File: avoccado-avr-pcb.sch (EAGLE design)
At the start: 31 parts, among them IC1 MCP1703CB, Q1 #MHz, Q2 MOSFET-NCHANNEL2N7002PW, U1 ATMEGA168#, U2 MCP73831, X1 Micro USB

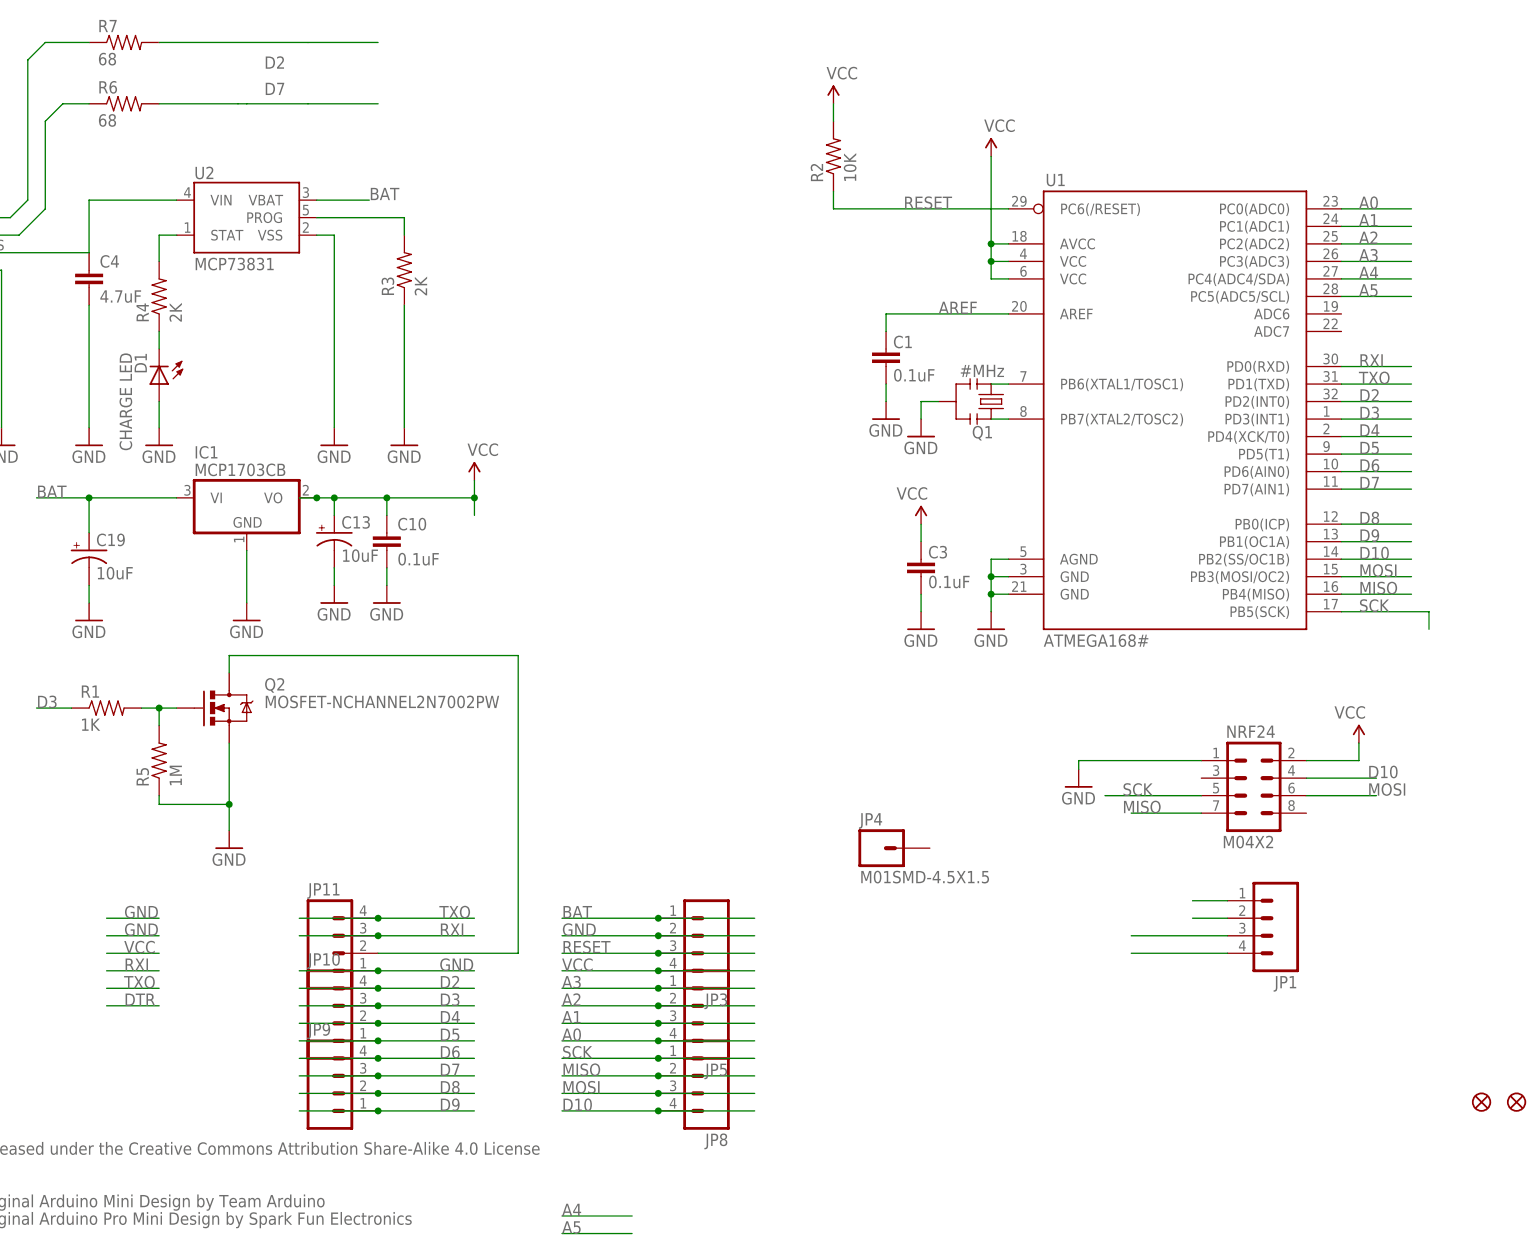
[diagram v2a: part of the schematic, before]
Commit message: white silkscreen fills at GND pads
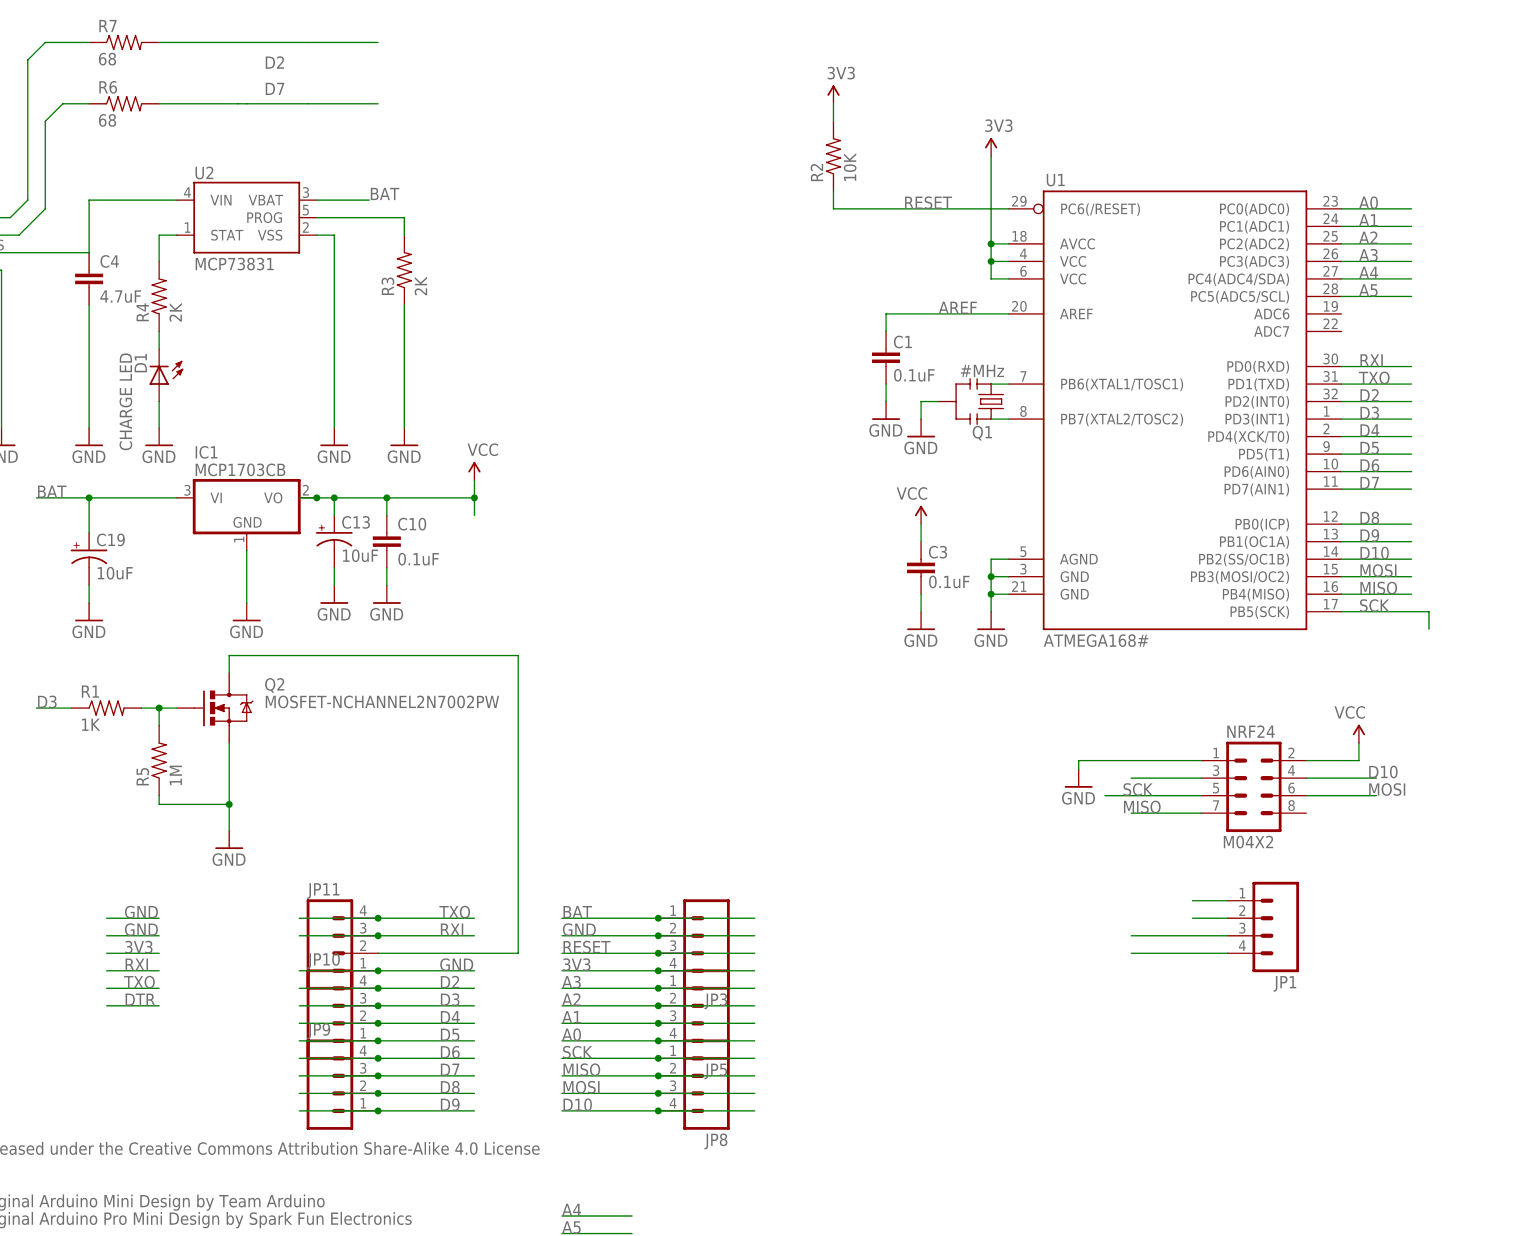
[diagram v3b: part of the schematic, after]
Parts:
- removed JP4: M01SMD-4.5X1.5, SparkFun-Connectors:M01SMD-4.5X1.5
- removed U$2, U$4: FIDUCIAL1X2, SparkFun:FIDUCIAL1X2
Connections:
- removed net 3.3V: NRF24.2
- removed net VCC: C10.1, C13.+, C3.2, IC1.VO, JP1.2, JP3.4, R2.2, U1.AVCC, U1.VCC@1, U1.VCC@2
- new net 3V3: C10.1, C13.+, C3.2, IC1.VO, JP1.2, JP3.4, NRF24.2, R2.2, U1.AVCC, U1.VCC@1, U1.VCC@2
- net D9: now also NRF24.3
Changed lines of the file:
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@@
 <part name="GND30" library="SparkFun" deviceset="GND" device=""/>
 <part name="GND32" library="SparkFun" deviceset="GND" device=""/>
-<part name="P+11" library="SparkFun" deviceset="3.3V" device="" value="VCC"/>
+<part name="P+11" library="SparkFun" deviceset="3.3V" device="" value="3V3"/>
 <part name="P+12" library="SparkFun" deviceset="3.3V" device="" value="VCC"/>
 <part name="P+15" library="SparkFun" deviceset="3.3V" device="" value="VCC"/>
-<part name="U$2" library="SparkFun" deviceset="FIDUCIAL" device="1X2"/>
-<part name="U$4" library="SparkFun" deviceset="FIDUCIAL" device="1X2"/>
 <part name="Q1" library="SparkFun" deviceset="RESONATOR" device="SMD" value="#MHz"/>
 <part name="GND4" library="SparkFun" deviceset="GND" device=""/>
 <part name="U1" library="SparkFun" deviceset="ATMEGA168" device="" value="ATMEGA168#"/>
-<part name="P+1" library="SparkFun" deviceset="3.3V" device="" value="VCC"/>
+<part name="P+1" library="SparkFun" deviceset="3.3V" device="" value="3V3"/>
 <part name="GND5" library="SparkFun" deviceset="GND" device=""/>
 <part name="Q2" library="SparkFun-DiscreteSemi" deviceset="MOSFET-NCHANNEL" device="2N7002PW"/>
@@
 <part name="GND9" library="SparkFun" deviceset="GND" device=""/>
 <part name="R5" library="SparkFun-Resistors" deviceset="RESISTOR" device="0603" value="1M"/>
-<part name="JP4" library="SparkFun-Connectors" deviceset="M01" device="SMD-4.5X1.5"/>
 <part name="JP3" library="smd-pads" deviceset="M04" device="SMD1X4"/>
 <part name="JP5" library="smd-pads" deviceset="M04" device="SMD1X4"/>
@@
 <attribute name="VALUE" x="151.384" y="112.776" size="1.778" layer="96"/>
 </instance>
-<instance part="U$2" gate="G$1" x="236.22" y="25.4"/>
-<instance part="U$4" gate="G$1" x="241.3" y="25.4"/>
 <instance part="Q1" gate="G$1" x="165.1" y="127" smashed="yes" rot="MR90">
 <attribute name="NAME" x="162.306" y="123.444" size="1.778" layer="95" rot="MR180"/>
@@
 <instance part="GND9" gate="1" x="54.61" y="62.23"/>
 <instance part="R5" gate="G$1" x="44.45" y="74.93" rot="R90"/>
-<instance part="JP4" gate="G$1" x="148.59" y="62.23"/>
 <instance part="JP3" gate="G$1" x="121.92" y="49.53" rot="R180"/>
 <instance part="JP5" gate="G$1" x="121.92" y="39.37" rot="R180"/>
@@
 </segment>
 </net>
-<net name="VCC" class="0">
+<net name="3V3" class="0">
 <segment>
 <wire x1="142.24" y1="170.18" x2="142.24" y2="167.64" width="0.1524" layer="91"/>
@@
 <pinref part="JP1" gate="G$1" pin="2"/>
 </segment>
+<segment>
+<pinref part="P+2" gate="G$1" pin="3.3V"/>
+<wire x1="218.44" y1="77.47" x2="218.44" y2="74.93" width="0.2032" layer="91"/>
+<pinref part="NRF24" gate="G$1" pin="2"/>
+<wire x1="218.44" y1="74.93" x2="210.82" y2="74.93" width="0.2032" layer="91"/>
+</segment>
 </net>
 <net name="D9" class="0">
@@
 <label x="218.44" y="106.68" size="1.778" layer="95"/>
 <pinref part="U1" gate="G$1" pin="PB1(OC1A)"/>
+</segment>
+<segment>
+<wire x1="185.42" y1="72.39" x2="195.58" y2="72.39" width="0.1524" layer="91"/>
+<pinref part="NRF24" gate="G$1" pin="3"/>
 </segment>
 </net>
@@
 </segment>
 </net>
-<net name="3.3V" class="0">
-<segment>
-<pinref part="P+2" gate="G$1" pin="3.3V"/>
-<wire x1="218.44" y1="77.47" x2="218.44" y2="74.93" width="0.2032" layer="91"/>
-<pinref part="NRF24" gate="G$1" pin="2"/>
-<wire x1="218.44" y1="74.93" x2="210.82" y2="74.93" width="0.2032" layer="91"/>
-</segment>
-</net>

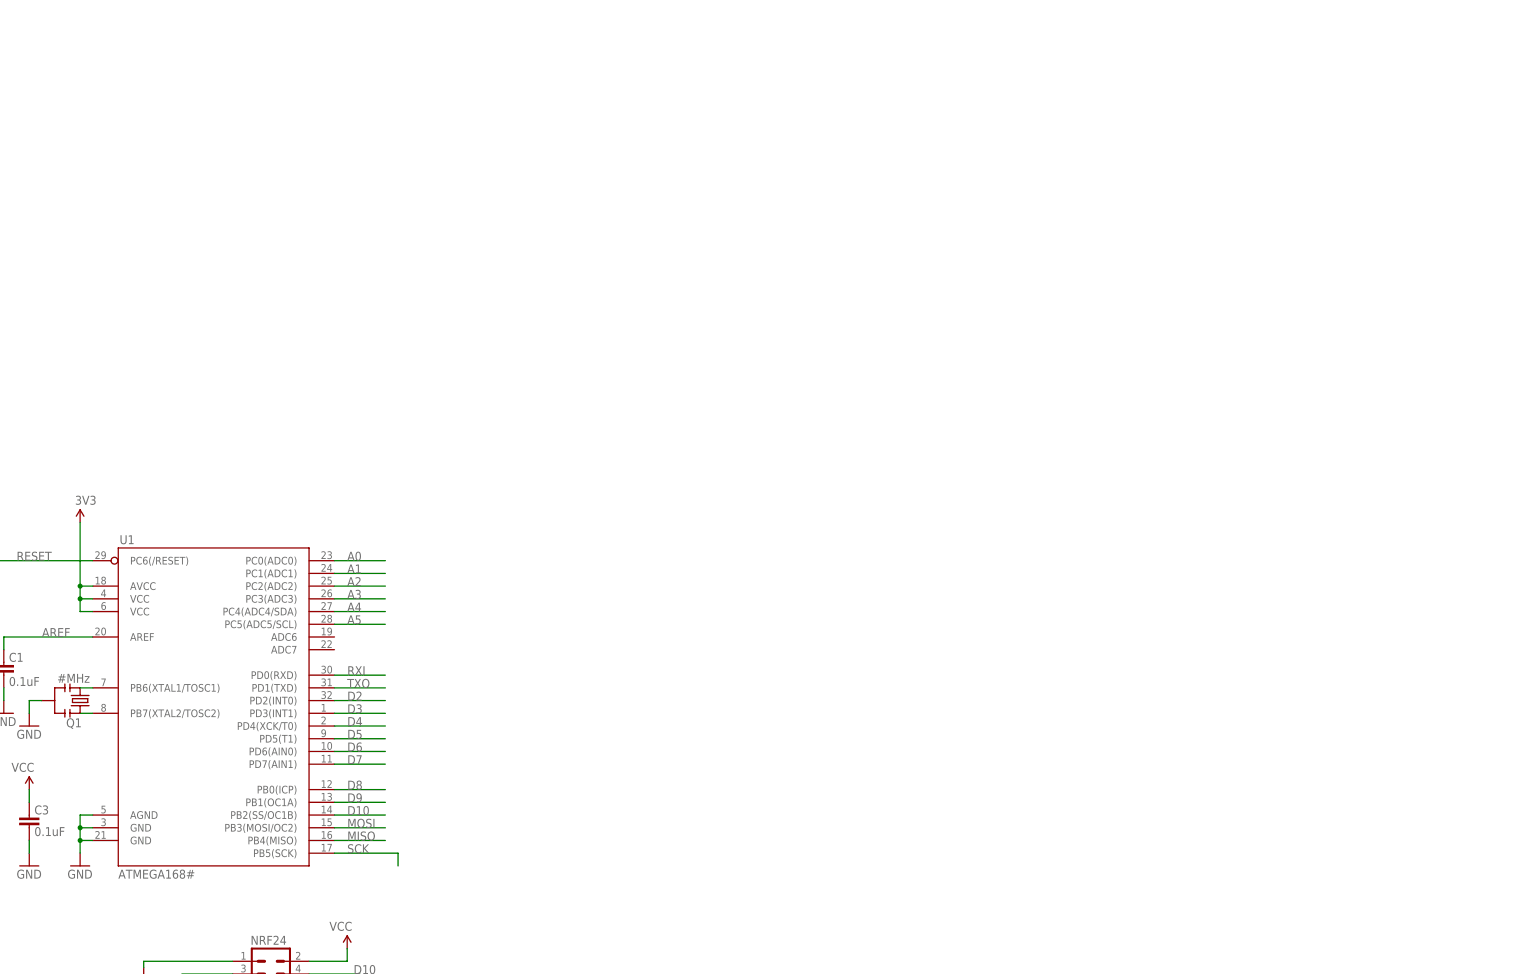
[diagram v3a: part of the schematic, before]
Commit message: add QFN package for MCU wip
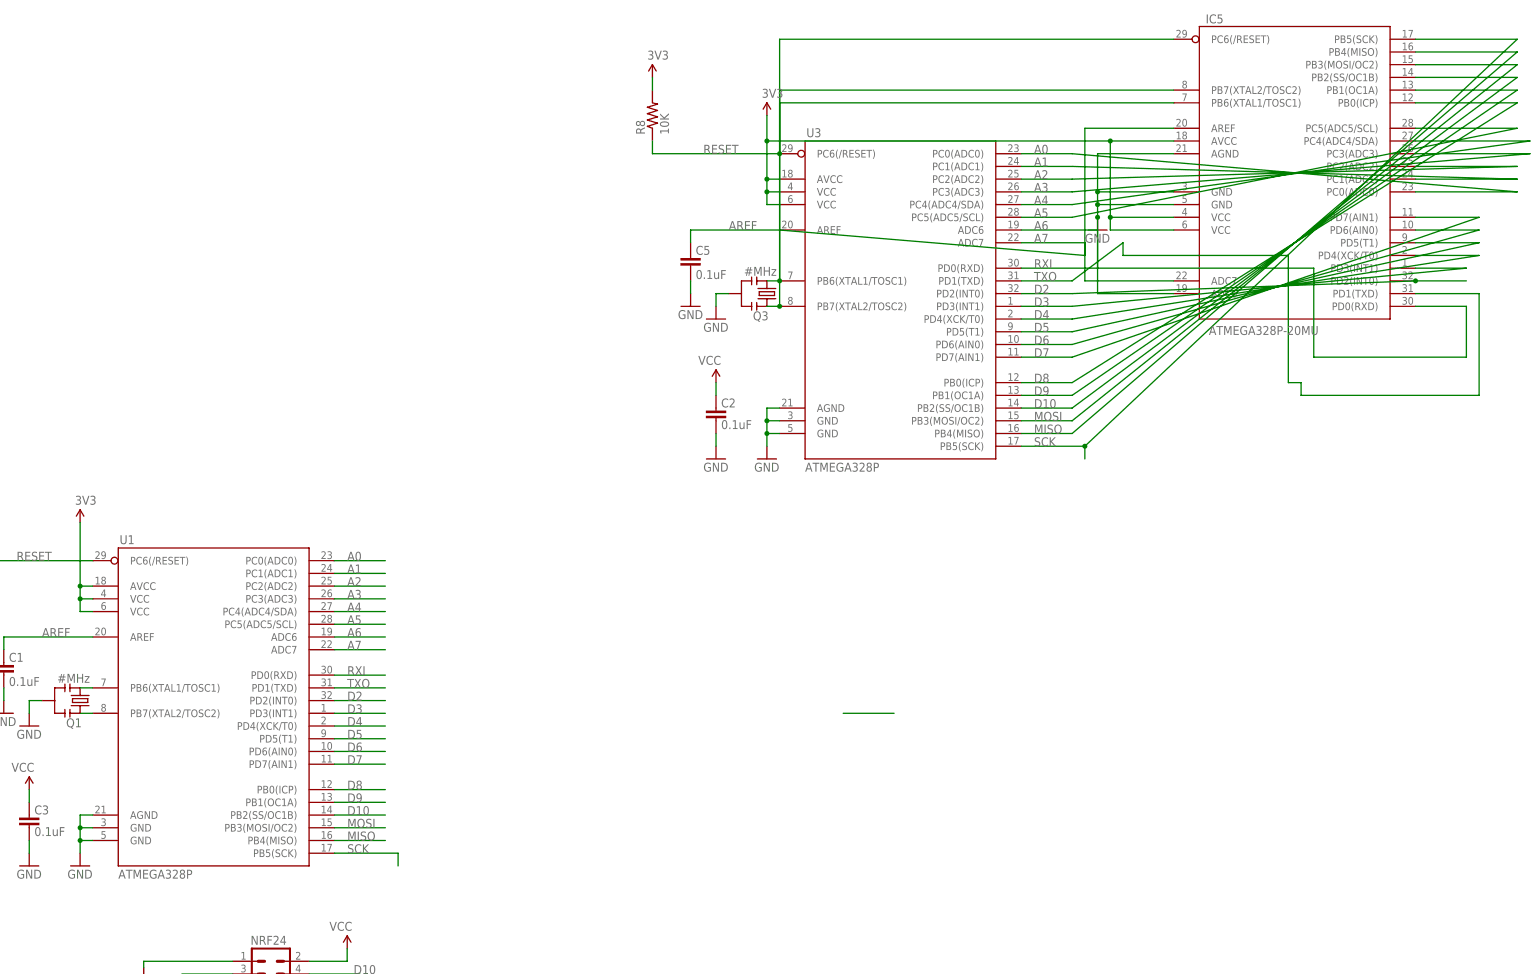
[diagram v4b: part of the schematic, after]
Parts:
- added C2, C5: 0.1uF, SparkFun:CAP0402
- added IC5: ATMEGA328P-20MU, idii:MEGA8-MI
- added Q3: #MHz, SparkFun:RESONATORSMD
- added R8: 10K, SparkFun-Resistors:RESISTOR0603
- added U3: ATMEGA328P, SparkFun-DigitalIC:ATMEGA328_SMT
- U1: value ATMEGA168# -> ATMEGA328P; device SparkFun:ATMEGA168 -> SparkFun-DigitalIC:ATMEGA328_SMT
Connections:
- new net A6: IC5.ADC6, U1.ADC6, U3.ADC6
- new net A7: IC5.ADC7, U1.ADC7, U3.ADC7
- new net N$10: IC5.PB7(XTAL2/TOSC2), Q3.3, U3.PB6(XTAL1/TOSC1)
- new net N$9: IC5.PB6(XTAL1/TOSC1), Q3.1, U3.PB7(XTAL2/TOSC2)
- net 3V3: now also C2.2, IC5.AVCC, IC5.VCC@1, IC5.VCC@2, R8.2, U3.AVCC, U3.VCC@1, U3.VCC@2
- net A0: now also IC5.PC0(ADC0), U3.PC0(ADC0)
- net A1: now also IC5.PC1(ADC1), U3.PC1(ADC1)
- net A2: now also IC5.PC2(ADC2), U3.PC2(ADC2)
- net A3: now also IC5.PC3(ADC3), U3.PC3(ADC3)
- net A4: now also IC5.PC4(ADC4/SDA), U3.PC4(ADC4/SDA)
- net A5: now also IC5.PC5(ADC5/SCL), U3.PC5(ADC5/SCL)
- net AREF: now also C5.2, IC5.AREF, U3.AREF
- net D10: now also IC5.PB2(SS/OC1B), U3.PB2(SS/OC1B)
- net D2: now also IC5.PD2(INT0), U3.PD2(INT0)
- net D3: now also IC5.PD3(INT1), U3.PD3(INT1)
- net D4: now also IC5.PD4(XCK/T0), U3.PD4(XCK/T0)
- net D5: now also IC5.PD5(T1), U3.PD5(T1)
- net D6: now also IC5.PD6(AIN0), U3.PD6(AIN0)
- net D7: now also IC5.PD7(AIN1), U3.PD7(AIN1)
- net D8: now also IC5.PB0(ICP), U3.PB0(ICP)
- net D9: now also IC5.PB1(OC1A), U3.PB1(OC1A)
- net GND: now also C2.1, C5.1, IC5.AGND, IC5.GND@1, IC5.GND@2, Q3.2, U3.AGND, U3.GND@1, U3.GND@2
- net MISO: now also IC5.PB4(MISO), U3.PB4(MISO)
- net MOSI: now also IC5.PB3(MOSI/OC2), U3.PB3(MOSI/OC2)
- net RESET: now also IC5.PC6(/RESET), R8.1, U3.PC6(/RESET)
- net RXI: now also IC5.PD0(RXD), U3.PD0(RXD)
- net SCK: now also IC5.PB5(SCK), U3.PB5(SCK)
- net TXO: now also IC5.PD1(TXD), U3.PD1(TXD)

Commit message: moved Xtal to make room for vias
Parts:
- removed C2, C5: 0.1uF, SparkFun:CAP0402
- removed Q3: #MHz, SparkFun:RESONATORSMD
- removed U3: ATMEGA328P, SparkFun-DigitalIC:ATMEGA328_SMT
- R8: value 10K -> 2K
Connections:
- net N$7 renamed USB-D+
- removed net N$10: IC5.PB7(XTAL2/TOSC2), Q3.3, U3.PB6(XTAL1/TOSC1)
- removed net N$8: R6.1, X1.D-
- new net USB-D-: R6.1, R8.1, X1.D-
- net 3V3: no longer C2.2, U3.AVCC, U3.VCC@1, U3.VCC@2
- net A0: no longer U3.PC0(ADC0)
- net A1: no longer U3.PC1(ADC1)
- net A2: no longer U3.PC2(ADC2)
- net A3: no longer U3.PC3(ADC3)
- net A4: no longer U3.PC4(ADC4/SDA)
- net A5: no longer U3.PC5(ADC5/SCL)
- net A6: no longer U3.ADC6
- net A7: no longer U3.ADC7
- net AREF: no longer C5.2, U3.AREF
- net D10: no longer U3.PB2(SS/OC1B)
- net D2: no longer U3.PD2(INT0)
- net D3: no longer U3.PD3(INT1)
- net D4: no longer U3.PD4(XCK/T0)
- net D5: no longer U3.PD5(T1)
- net D6: no longer U3.PD6(AIN0)
- net D7: no longer U3.PD7(AIN1)
- net D8: no longer U3.PB0(ICP)
- net D9: no longer U3.PB1(OC1A)
- net GND: no longer C2.1, C5.1, Q3.2, U3.AGND, U3.GND@1, U3.GND@2
- net MISO: no longer U3.PB4(MISO)
- net MOSI: no longer U3.PB3(MOSI/OC2)
- net N$1: now also IC5.PB7(XTAL2/TOSC2)
- net N$2: now also IC5.PB6(XTAL1/TOSC1)
- net N$9: now also IC5.PD1(TXD); no longer IC5.PB6(XTAL1/TOSC1), Q3.1, U3.PB7(XTAL2/TOSC2)
- net RESET: no longer R8.1, U3.PC6(/RESET)
- net RXI: no longer U3.PD0(RXD)
- net SCK: no longer U3.PB5(SCK)
- net TXO: no longer IC5.PD1(TXD), U3.PD1(TXD)
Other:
- moved on the sheet: IC5, R8
